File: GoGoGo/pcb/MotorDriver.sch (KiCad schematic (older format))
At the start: 9 parts, among them P101 CONN_01X02, P102 CONN_01X04, P103 CONN_01X02, P104 CONN_01X02, U101 TB6593FNG

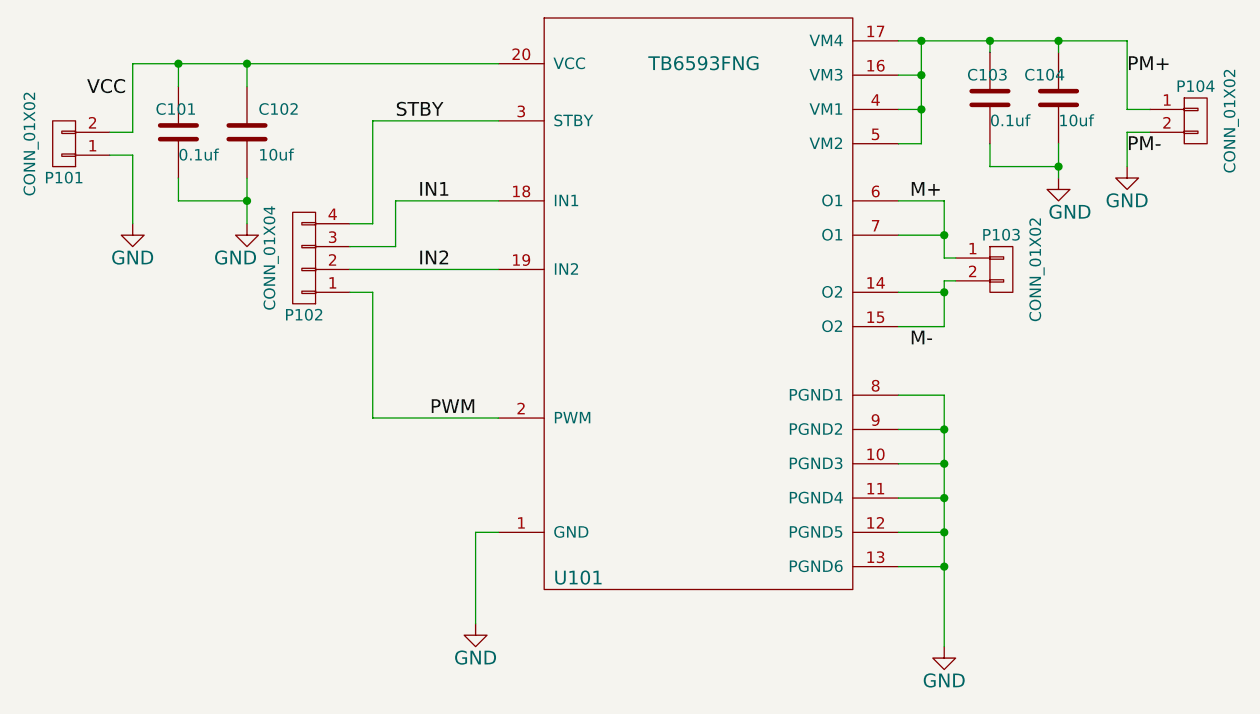
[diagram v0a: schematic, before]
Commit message: MotorDriver pcb rough layout
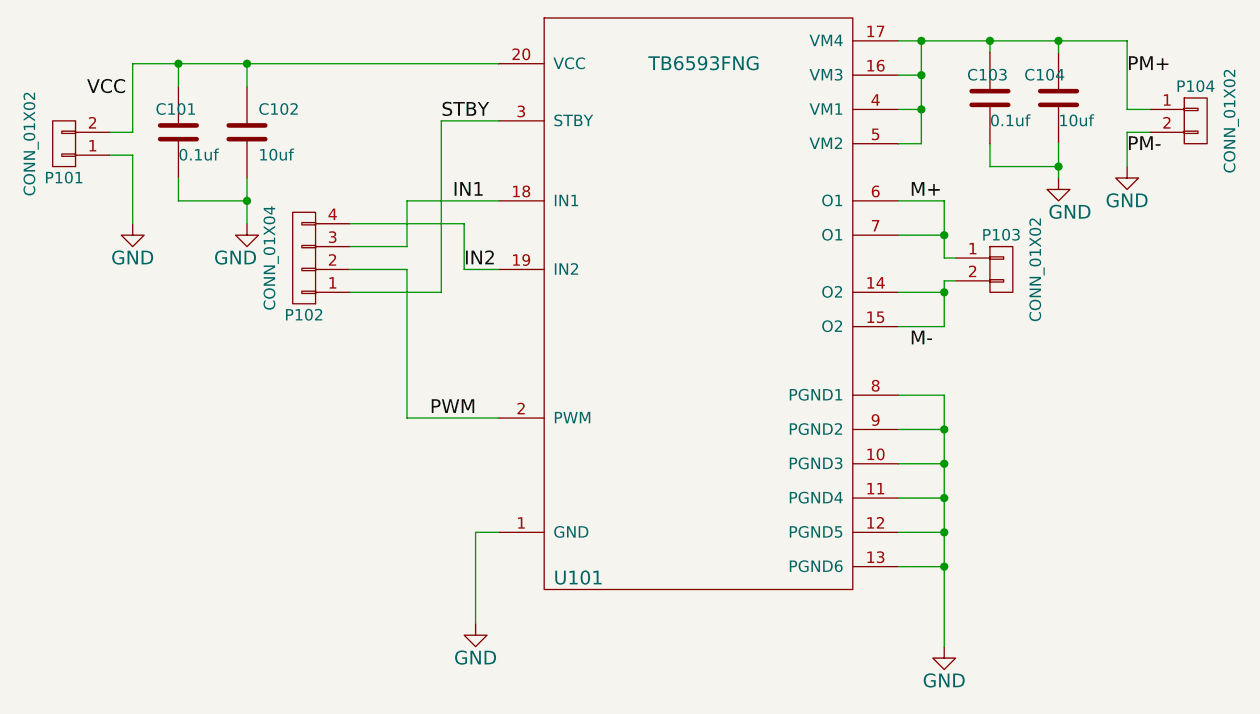
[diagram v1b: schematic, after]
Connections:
- net IN2: now also P102.4 (P4); no longer P102.2 (P2)
- net PWM: now also P102.2 (P2); no longer P102.1 (P1)
- net STBY: now also P102.1 (P1); no longer P102.4 (P4)
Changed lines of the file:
@@
 encoding utf-8
 Sheet 1 1
-Title ""
+Title "GoGoGo Motor Driver"
 Date ""
 Rev ""
@@
 $EndComp
 Wire Wire Line
-	2000 2650 2000 2200
-Wire Wire Line
-	2000 2200 2550 2200
-Wire Wire Line
-	1900 2650 2000 2650
-Wire Wire Line
-	1900 2750 2100 2750
-Wire Wire Line
-	2100 2750 2100 2550
-Wire Wire Line
-	2100 2550 2550 2550
-Wire Wire Line
-	1900 2850 2550 2850
-Wire Wire Line
-	1900 2950 2000 2950
-Wire Wire Line
-	2000 2950 2000 3500
-Wire Wire Line
-	2000 3500 2550 3500
-Text Label 2100 2200 0    60   ~ 0
-STBY
-Text Label 2200 2550 0    60   ~ 0
-IN1
-Text Label 2200 2850 0    60   ~ 0
-IN2
-Text Label 2250 3500 0    60   ~ 0
-PWM
-Wire Wire Line
 	2550 1950 950  1950
 Wire Wire Line
@@
 	1    0    0    -1
 $EndComp
+Wire Wire Line
+	1900 2650 2400 2650
+Wire Wire Line
+	2400 2650 2400 2850
+Wire Wire Line
+	2400 2850 2550 2850
+Wire Wire Line
+	1900 2750 2150 2750
+Wire Wire Line
+	2150 2750 2150 2550
+Wire Wire Line
+	2150 2550 2550 2550
+Wire Wire Line
+	1900 2950 2300 2950
+Wire Wire Line
+	2300 2950 2300 2200
+Wire Wire Line
+	2300 2200 2550 2200
+Wire Wire Line
+	1900 2850 2150 2850
+Wire Wire Line
+	2150 2850 2150 3500
+Wire Wire Line
+	2150 3500 2550 3500
+Text Label 2300 2200 0    60   ~ 0
+STBY
+Text Label 2350 2550 0    60   ~ 0
+IN1
+Text Label 2400 2850 0    60   ~ 0
+IN2
+Text Label 2250 3500 0    60   ~ 0
+PWM
 $EndSCHEMATC
